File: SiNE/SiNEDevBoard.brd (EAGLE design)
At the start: 40 x 45 mm, 33 parts, among them IC1 ATTINY24/44/84-SSU, IC2 74HC164D, J1 AVR_SPI_PRG_6NS

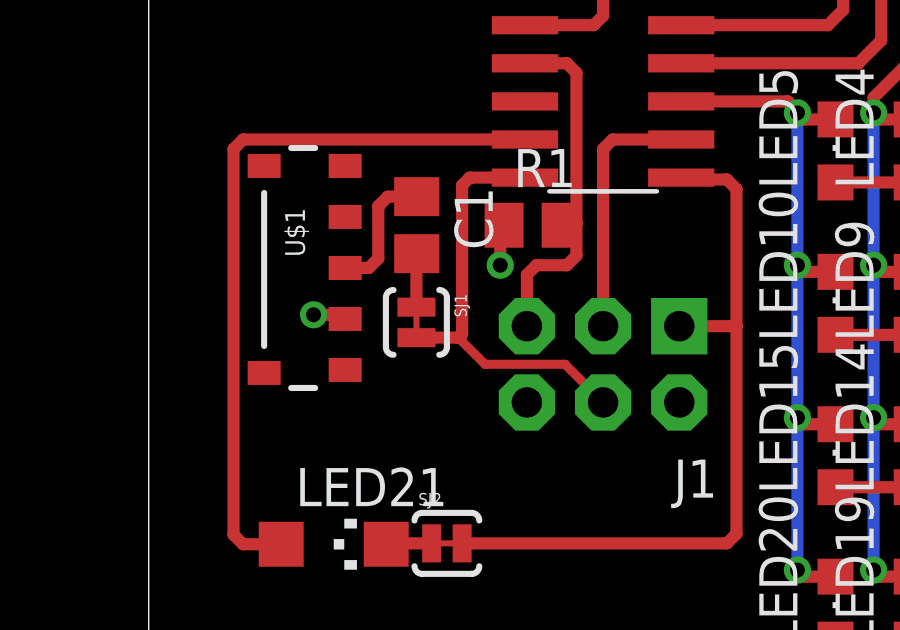
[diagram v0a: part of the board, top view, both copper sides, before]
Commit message: added v0.1 gerbers and new images
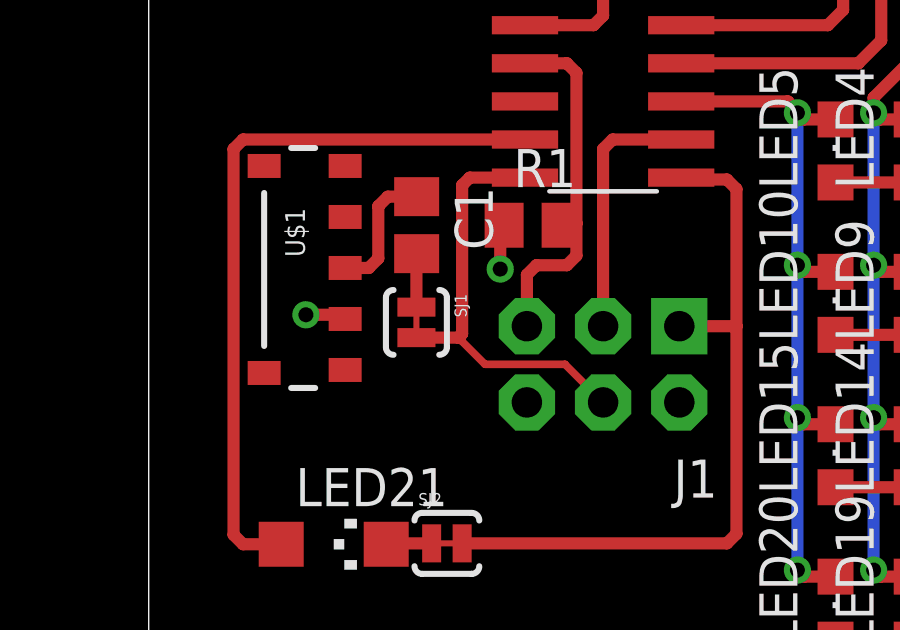
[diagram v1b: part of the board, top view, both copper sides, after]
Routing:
- net VCC: track 10.2 -> 11.0 mm
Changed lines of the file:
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@@
 <setting verticaltext="up"/>
 </settings>
-<grid distance="5" unitdist="mm" unit="mm" style="lines" multiple="1" display="yes" altdistance="0.025" altunitdist="inch" altunit="inch"/>
+<grid distance="5" unitdist="mil" unit="mil" style="lines" multiple="1" display="yes" altdistance="0.025" altunitdist="inch" altunit="inch"/>
 <layers>
-<layer number="1" name="Top" color="4" fill="1" visible="yes" active="yes"/>
+<layer number="1" name="Top" color="4" fill="1" visible="no" active="yes"/>
 <layer number="16" name="Bottom" color="1" fill="1" visible="yes" active="yes"/>
 <layer number="17" name="Pads" color="2" fill="1" visible="yes" active="yes"/>
@@
 <layer number="19" name="Unrouted" color="6" fill="1" visible="yes" active="yes"/>
 <layer number="20" name="Dimension" color="15" fill="1" visible="yes" active="yes"/>
-<layer number="21" name="tPlace" color="7" fill="1" visible="yes" active="yes"/>
+<layer number="21" name="tPlace" color="7" fill="1" visible="no" active="yes"/>
 <layer number="22" name="bPlace" color="7" fill="1" visible="yes" active="yes"/>
-<layer number="23" name="tOrigins" color="15" fill="1" visible="yes" active="yes"/>
+<layer number="23" name="tOrigins" color="15" fill="1" visible="no" active="yes"/>
 <layer number="24" name="bOrigins" color="15" fill="1" visible="yes" active="yes"/>
-<layer number="25" name="tNames" color="7" fill="1" visible="yes" active="yes"/>
-<layer number="26" name="bNames" color="7" fill="1" visible="yes" active="yes"/>
-<layer number="27" name="tValues" color="7" fill="1" visible="yes" active="yes"/>
-<layer number="28" name="bValues" color="7" fill="1" visible="yes" active="yes"/>
+<layer number="25" name="tNames" color="7" fill="1" visible="no" active="yes"/>
+<layer number="26" name="bNames" color="7" fill="1" visible="no" active="yes"/>
+<layer number="27" name="tValues" color="7" fill="1" visible="no" active="yes"/>
+<layer number="28" name="bValues" color="7" fill="1" visible="no" active="yes"/>
 <layer number="29" name="tStop" color="7" fill="3" visible="no" active="yes"/>
 <layer number="30" name="bStop" color="7" fill="6" visible="no" active="yes"/>
@@
 <layer number="37" name="tTest" color="7" fill="1" visible="no" active="yes"/>
 <layer number="38" name="bTest" color="7" fill="1" visible="no" active="yes"/>
-<layer number="39" name="tKeepout" color="4" fill="11" visible="yes" active="yes"/>
+<layer number="39" name="tKeepout" color="4" fill="11" visible="no" active="yes"/>
 <layer number="40" name="bKeepout" color="1" fill="11" visible="yes" active="yes"/>
-<layer number="41" name="tRestrict" color="4" fill="10" visible="yes" active="yes"/>
+<layer number="41" name="tRestrict" color="4" fill="10" visible="no" active="yes"/>
 <layer number="42" name="bRestrict" color="1" fill="10" visible="yes" active="yes"/>
 <layer number="43" name="vRestrict" color="2" fill="10" visible="yes" active="yes"/>
@@
 <layer number="49" name="Reference" color="7" fill="1" visible="yes" active="yes"/>
 <layer number="50" name="dxf" color="7" fill="1" visible="no" active="no"/>
-<layer number="51" name="tDocu" color="7" fill="1" visible="yes" active="yes"/>
+<layer number="51" name="tDocu" color="7" fill="1" visible="no" active="yes"/>
 <layer number="52" name="bDocu" color="7" fill="1" visible="yes" active="yes"/>
 <layer number="53" name="tGND_GNDA" color="7" fill="9" visible="no" active="no"/>
@@
 <wire x1="32.7355" y1="25.908" x2="32.7355" y2="26.2255" width="0.4064" layer="16"/>
 <wire x1="11.8465" y1="16.4465" x2="11.717" y2="16.317" width="0.4064" layer="1"/>
-<wire x1="11.717" y1="16.317" x2="11.717" y2="15.113" width="0.4064" layer="1"/>
-<via x="11.717" y="15.113" extent="1-16" drill="0.5"/>
-<wire x1="11.717" y1="15.113" x2="11.717" y2="15.24" width="0.4064" layer="16"/>
+<wire x1="11.717" y1="16.317" x2="11.717" y2="14.986" width="0.4064" layer="1"/>
+<via x="11.717" y="14.986" extent="1-16" drill="0.5"/>
+<wire x1="11.717" y1="14.986" x2="11.717" y2="15.24" width="0.4064" layer="16"/>
 <wire x1="12.5425" y1="25.654" x2="12.479" y2="25.7175" width="0.4064" layer="1"/>
 <wire x1="12.479" y1="25.7175" x2="12.479" y2="27.051" width="0.4064" layer="1"/>
@@
 <wire x1="12.479" y1="27.051" x2="12.479" y2="26.924" width="0.4064" layer="16"/>
 <wire x1="6.548" y1="13.322" x2="6.408" y2="13.462" width="0.4064" layer="1"/>
-<wire x1="6.408" y1="13.462" x2="5.494" y2="13.462" width="0.4064" layer="1"/>
-<via x="5.494" y="13.462" extent="1-16" drill="0.5"/>
-<wire x1="5.494" y1="13.462" x2="5.621" y2="13.462" width="0.4064" layer="16"/>
+<wire x1="6.408" y1="13.462" x2="5.24" y2="13.462" width="0.4064" layer="1"/>
+<via x="5.24" y="13.462" extent="1-16" drill="0.5"/>
+<wire x1="5.24" y1="13.462" x2="5.621" y2="13.462" width="0.4064" layer="16"/>
 </signal>
 <signal name="MOSI">
 <contactref element="J1" pad="4"/>
 <contactref element="IC1" pad="7"/>
-<wire x1="15.146" y1="10.541" x2="13.876" y2="11.811" width="0.3048" layer="1"/>
-<wire x1="13.876" y1="11.811" x2="11.209" y2="11.811" width="0.3048" layer="1"/>
-<wire x1="11.209" y1="11.811" x2="10.447" y2="12.573" width="0.3048" layer="1"/>
-<wire x1="10.447" y1="12.573" x2="10.447" y2="12.827" width="0.3048" layer="1"/>
+<wire x1="15.146" y1="10.541" x2="13.876" y2="11.811" width="0.254" layer="1"/>
+<wire x1="13.876" y1="11.811" x2="11.209" y2="11.811" width="0.254" layer="1"/>
+<wire x1="11.209" y1="11.811" x2="10.447" y2="12.573" width="0.254" layer="1"/>
+<wire x1="10.447" y1="12.573" x2="10.447" y2="12.827" width="0.254" layer="1"/>
 <wire x1="10.447" y1="12.827" x2="10.447" y2="17.78" width="0.4064" layer="1"/>
 <wire x1="10.447" y1="17.78" x2="10.701" y2="18.034" width="0.4064" layer="1"/>
@@
 </signal>
 </signals>
+<errors>
+</errors>
 </board>
 </drawing>
